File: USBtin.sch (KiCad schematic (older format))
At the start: 20 parts, among them J1 USB_B, J2 Conn_01x03, U1 PIC18F14K50-EP, U2 MCP2515, U3 MCP2561-E-P, Y1 24MHz

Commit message: schematic and pcb done
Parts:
- removed U2: MCP2515, symbol Libabar:MCP2515
- removed U3: MCP2561-E-P, Package_DIP:DIP-8_W7.62mm, symbol Interface_CAN_LIN:MCP2561-E-P
- added C7: 100n, Capacitor_THT:C_Disc_D5.1mm_W3.2mm_P5.00mm, symbol Device:C
- added IC1: MCP2515-I_P, Package_DIP:DIP-18_W7.62mm, symbol villanut_lib:MCP2515-I_P
- added U2: MCP2551-I-P, Package_DIP:DIP-8_W7.62mm, symbol Interface_CAN_LIN:MCP2551-I-P
- C1, C2, C3: footprint (none) -> Capacitor_THT:C_Disc_D5.1mm_W3.2mm_P5.00mm
- C4: footprint (none) -> Capacitor_THT:CP_Radial_D5.0mm_P2.50mm
- C5, C6: footprint (none) -> Capacitor_THT:C_Disc_D3.4mm_W2.1mm_P2.50mm
- D1: value D -> red; footprint (none) -> LED_THT:LED_D3.0mm
- J1: footprint (none) -> Connector_USB:USB_B_OST_USB-B1HSxx_Horizontal
- J2: footprint (none) -> TerminalBlock_RND:TerminalBlock_RND_205-00002_1x03_P5.00mm_Horizontal
- JP1, JP2: footprint (none) -> Connector_PinHeader_2.54mm:PinHeader_1x02_P2.54mm_Vertical
- R1, R2, R3, R4, R5: footprint (none) -> Resistor_THT:R_Axial_DIN0411_L9.9mm_D3.6mm_P5.08mm_Vertical
- Y1: footprint (none) -> Crystal:Crystal_HC49-U_Vertical
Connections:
- wire segments 95 -> 98
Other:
- note added: "Tester avec RS\ndirect sur GND"
- moved on the sheet: R5

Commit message: changing C4 to a polarize capacitor
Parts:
- removed C4: 4.7u, Capacitor_THT:CP_Radial_D5.0mm_P2.50mm, symbol Device:C
- added C4: 4.7u, Capacitor_THT:CP_Radial_D5.0mm_P2.50mm, symbol Device:CP
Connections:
- net +5V: now also C4.1
- net GND: now also C4.2
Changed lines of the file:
@@
 Wire Wire Line
 	2400 4100 2250 4100
-$Comp
-L Device:C C4
-U 1 1 5DB4DA9B
-P 4500 1350
-F 0 "C4" H 4615 1396 50  0000 L CNN
-F 1 "4.7u" H 4615 1305 50  0000 L CNN
-F 2 "Capacitor_THT:CP_Radial_D5.0mm_P2.50mm" H 4538 1200 50  0001 C CNN
-F 3 "~" H 4500 1350 50  0001 C CNN
-	1    4500 1350
-	1    0    0    -1
-$EndComp
 Wire Wire Line
 	4500 1500 4500 1600
@@
 Text Notes 6750 5150 0    50   ~ 0
 Tester avec RS\ndirect sur GND
+$Comp
+L Device:CP C4
+U 1 1 5DB097F7
+P 4500 1350
+F 0 "C4" H 4618 1396 50  0000 L CNN
+F 1 "4.7u" H 4618 1305 50  0000 L CNN
+F 2 "Capacitor_THT:CP_Radial_D5.0mm_P2.50mm" H 4538 1200 50  0001 C CNN
+F 3 "~" H 4500 1350 50  0001 C CNN
+	1    4500 1350
+	1    0    0    -1
+$EndComp
 $EndSCHEMATC

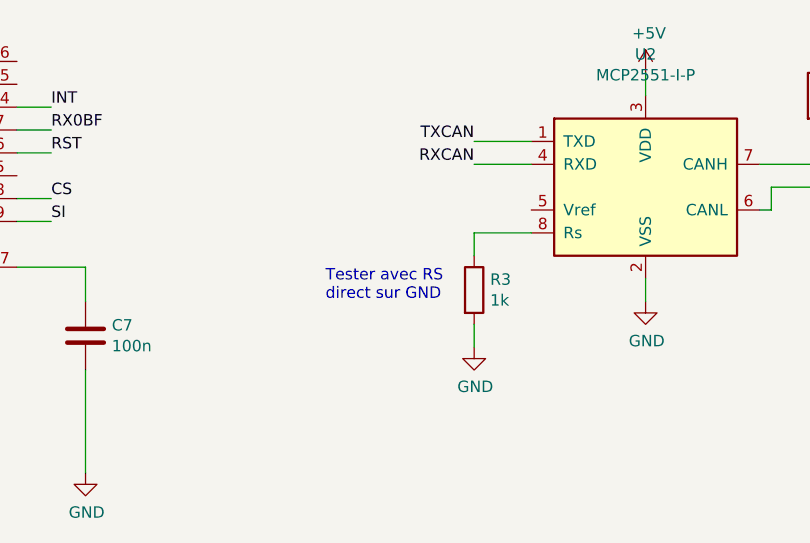
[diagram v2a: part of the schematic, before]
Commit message: removing comment on schematic
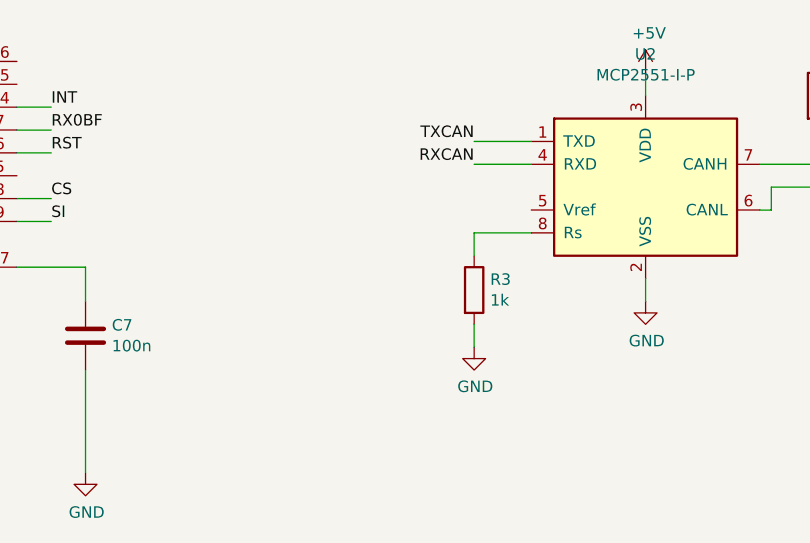
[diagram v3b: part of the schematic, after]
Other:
- note removed: "Tester avec RS\ndirect sur GND"
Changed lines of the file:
@@
 Wire Wire Line
 	5700 5000 5400 5000
-Text Notes 6750 5150 0    50   ~ 0
-Tester avec RS\ndirect sur GND
 $Comp
 L Device:CP C4
